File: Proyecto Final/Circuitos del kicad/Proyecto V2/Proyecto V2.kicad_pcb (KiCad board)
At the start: 2 copper layers, 259.8 x 173.7 mm, 43 parts, among them J1 12v, Q1 PN2222A, Q2 PN2222A, Q3 PN2222A, SW1 SW_Push, SW2 SW_Push, SW3 SW_Push, SW4 SW_Push, U1 LM7805, U3 ATmega328P-P, Y1 16MHz

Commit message: Cambios plaqueta
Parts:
- R2, R3, R4: value 1k -> 4k7
- moved D2 10.2 mm to (61.7, 136.7), turned to 180 degrees
- moved D3 10.2 mm to (61.7, 130.0), turned to 180 degrees
- moved D1 10.1 mm to (61.8, 143.5), turned to 180 degrees
- moved Encoder/puls-arduino1 8.63 mm to (17.2, 47.6)
- moved ESP2866-2 7.67 mm to (127.8, 78.9), turned to 90 degrees
- moved Y1 7.17 mm to (31.3, 53.9)
- moved C2 7.08 mm to (27.7, 64.2)
- moved C1 7.08 mm to (27.7, 48.4)
- moved ESP2866-arduino1 6.15 mm to (43.3, 27.9), turned to 90 degrees
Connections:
- D1 pad 1: Net-(D1-Pad1) -> +12V
- D1 pad 2: +12V -> Net-(Q3-Pad3)
- D2 pad 1: Net-(D2-Pad1) -> +12V
- D2 pad 2: +12V -> Net-(Q2-Pad3)
- D3 pad 1: Net-(D3-Pad1) -> +12V
- D3 pad 2: +12V -> Net-(Relay-3-PadA2)
- ESP2866-2 pad 3: Net-(ESP2866-2-Pad3) -> Net-(ESP8266-Pad18)
- ESP8266 pad 18: Net-(ESP2866-2-Pad2) -> Net-(ESP8266-Pad18)
- ESP8266 pad 19: Net-(ESP2866-2-Pad3) -> Net-(ESP2866-2-Pad2)
- Encoder/puls-arduino1 pad 3: Net-(Encoder/puls-arduino1-Pad3) -> Net-(U3-Pad5)
- Encoder/puls-arduino1 pad 5: Net-(Encoder/puls-arduino1-Pad5) -> Net-(U3-Pad4)
- Q1 pad 3: Net-(D3-Pad1) -> Net-(Relay-3-PadA2)
- Q2 pad 3: Net-(D2-Pad1) -> Net-(Q2-Pad3)
- Q3 pad 3: Net-(D1-Pad1) -> Net-(Q3-Pad3)
- Relay-1 pad A1: Net-(D1-Pad1) -> +12V
- Relay-1 pad A2: GND -> Net-(Q3-Pad3)
- Relay-2 pad A1: Net-(D2-Pad1) -> +12V
- Relay-2 pad A2: GND -> Net-(Q2-Pad3)
- Relay-3 pad A1: Net-(D3-Pad1) -> +12V
- Relay-3 pad A2: GND -> Net-(Relay-3-PadA2)
- U3 pad 4: Net-(Encoder/puls-arduino1-Pad3) -> Net-(U3-Pad4)
- U3 pad 5: Net-(Encoder/puls-arduino1-Pad5) -> Net-(U3-Pad5)
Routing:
- net +12V: track 97.9 -> 210.9 mm
- net Net-(D3-Pad1): track 66.6 -> 0.00 mm
- net Net-(Encoder/puls-arduino1-Pad5): track 60.7 -> 0.00 mm
- net Net-(Q3-Pad3): track 0.00 -> 53.4 mm
- net Net-(Encoder/puls-arduino1-Pad3): track 48.3 -> 0.00 mm
- net Net-(U3-Pad4): track 0.00 -> 43.7 mm
- net Net-(D1-Pad1): track 41.8 -> 0.00 mm
- net Net-(U3-Pad5): track 0.00 -> 36.5 mm
- net Net-(Q2-Pad3): track 0.00 -> 35.2 mm
- net Net-(D2-Pad1): track 35.1 -> 0.00 mm
- net Net-(ESP2866-2-Pad3): track 33.3 -> 0.00 mm
- net Net-(Relay-3-PadA2): track 0.00 -> 29.7 mm
- net Net-(ESP8266-Pad18): track 0.00 -> 29.4 mm
- net Net-(Encoder/puls-arduino1-Pad4): track 19.1 -> 27.8 mm
- net Net-(Encoder/puls-arduino1-Pad7): track 142.1 -> 150.7 mm
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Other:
- board size 259.8 x 173.7 mm -> 279.3 x 173.7 mm
- board text added: "+"

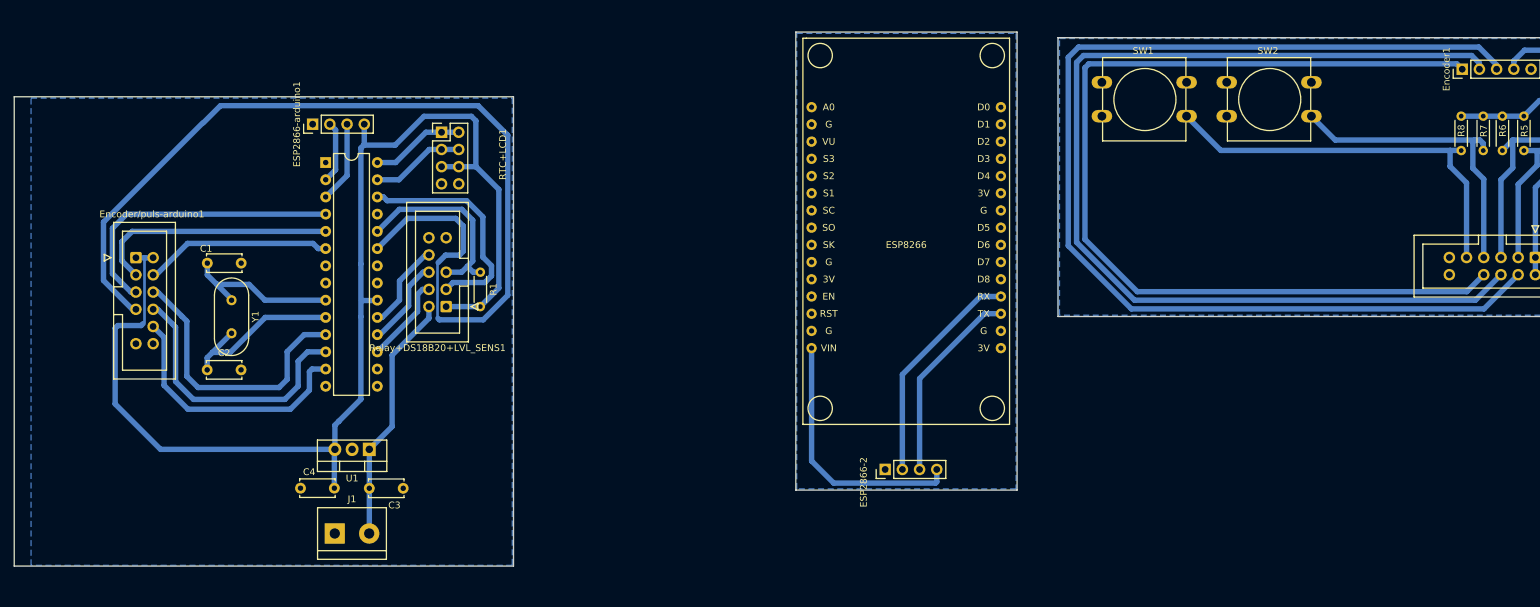
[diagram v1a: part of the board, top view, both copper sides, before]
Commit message: IDC ESP + reset
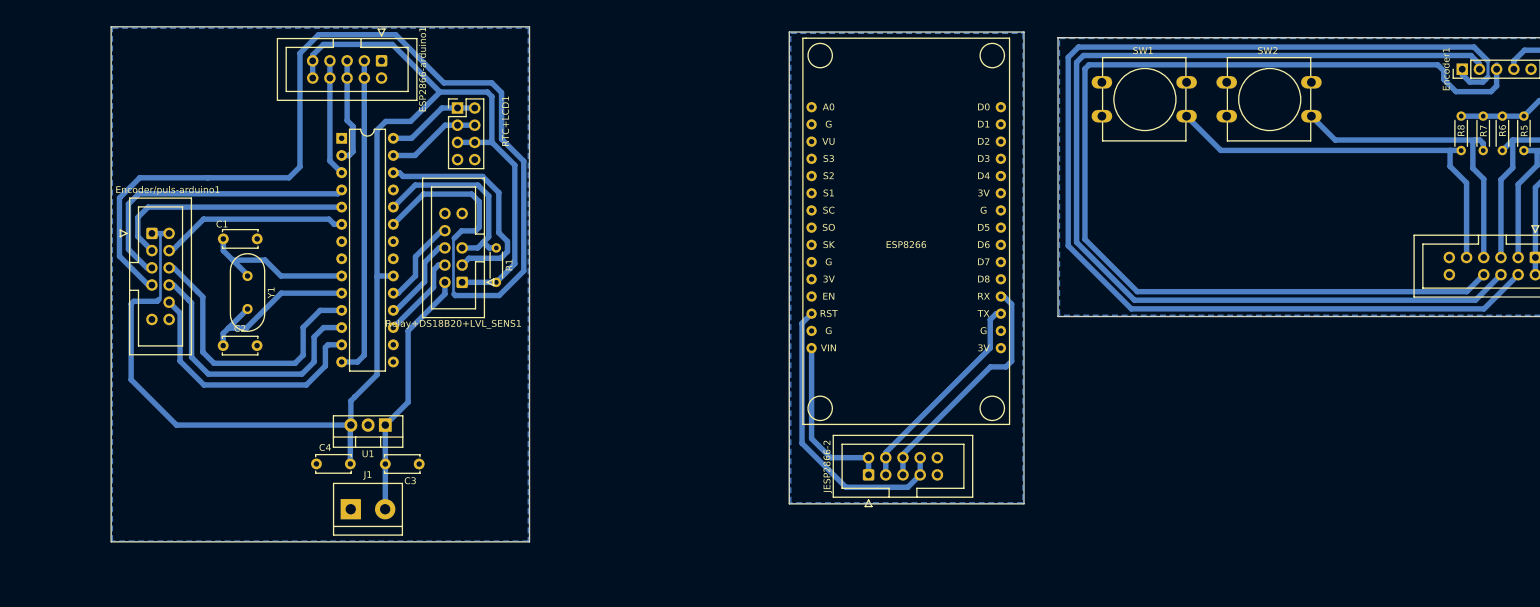
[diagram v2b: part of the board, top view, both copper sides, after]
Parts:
- removed ESP2866-2: Conn_01x04, Connector_PinHeader_2.54mm:PinHeader_1x04_P2.54mm_Vertical
- added JESP2866-2: Conn_02x05_Odd_Even, Connector_IDC:IDC-Header_2x05_P2.54mm_Vertical, F.Cu at (125.3, 79.7)
- ESP2866-arduino1: value Conn_01x04 -> Conn_02x05_Odd_Even; footprint Connector_PinHeader_2.54mm:PinHeader_1x04_P2.54mm_Vertical -> Connector_IDC:IDC-Header_2x05_P2.54mm_Vertical
- moved ESP2866-arduino1 13.8 mm to (53.4, 18.6), turned to -90 degrees
- moved C2 4.29 mm to (30.1, 60.6)
- moved Relay+DS18B20+LVL_SENS1 4.29 mm to (65.3, 51.3)
- moved J1 4.29 mm to (48.9, 84.8)
- moved C1 4.29 mm to (30.1, 44.9)
- moved C3 4.29 mm to (59.0, 78.1)
- moved C4 4.29 mm to (43.8, 78.1)
- moved Encoder/puls-arduino1 4.29 mm to (19.5, 44.0)
- moved R1 4.29 mm to (70.4, 46.2)
- moved RTC+LCD1 4.29 mm to (64.7, 25.5)
- moved U1 4.29 mm to (54.0, 72.3)
- moved U3 4.29 mm to (47.6, 30.0)
- moved Y1 4.29 mm to (33.7, 50.3)
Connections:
- ESP2866-arduino1 pad 2: Net-(ESP2866-arduino1-Pad2) -> GND
- ESP2866-arduino1 pad 3: Net-(ESP2866-arduino1-Pad3) -> Net-(U3-Pad14)
- ESP2866-arduino1 pad 4: +5V -> Net-(U3-Pad14)
- ESP8266 pad 13: unconnected-(ESP8266-Pad13) -> Net-(ESP8266-Pad13)
- Encoder/puls2 pad 4: Net-(Encoder/puls2-Pad4) -> Net-(Encoder1-Pad1)
- Encoder1 pad 1: Net-(Encoder/puls2-Pad8) -> Net-(Encoder1-Pad1)
- Encoder1 pad 3: Net-(Encoder/puls2-Pad4) -> Net-(Encoder/puls2-Pad8)
- U3 pad 14: unconnected-(U3-Pad14) -> Net-(U3-Pad14)
- U3 pad 2: Net-(ESP2866-arduino1-Pad2) -> Net-(U3-Pad2)
- U3 pad 3: Net-(ESP2866-arduino1-Pad3) -> Net-(U3-Pad3)
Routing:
- net Net-(Encoder1-Pad1): track 0.00 -> 171.3 mm
- net Net-(Encoder/puls2-Pad4): track 165.7 -> 0.00 mm
- net Net-(U3-Pad14): track 0.00 -> 47.2 mm
- net Net-(ESP8266-Pad13): track 0.00 -> 43.1 mm
- net Net-(U3-Pad3): track 0.00 -> 17.7 mm
- net Net-(U3-Pad2): track 0.00 -> 15.7 mm
- net Net-(Encoder/puls-arduino1-Pad7): track 150.7 -> 166.1 mm
- net Net-(ESP2866-arduino1-Pad3): track 12.0 -> 0.00 mm
- net Net-(Encoder/puls2-Pad8): track 144.7 -> 155.1 mm
- net +5V: track 570.7 -> 580.0 mm
- net Net-(ESP2866-arduino1-Pad2): track 9.16 -> 0.00 mm
- net Net-(ESP8266-Pad19): track 33.4 -> 35.2 mm
- net Net-(ESP8266-Pad18): track 29.4 -> 31.2 mm
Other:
- board size 279.3 x 173.7 mm -> 265 x 174.5 mm

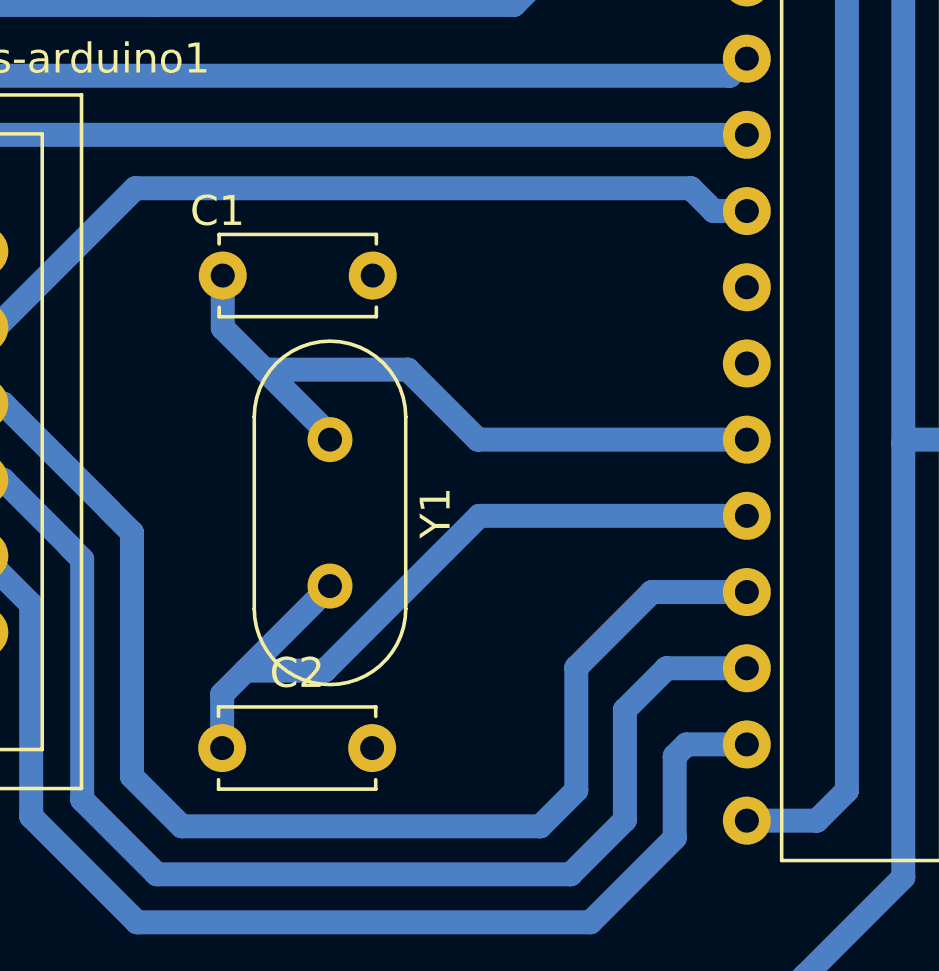
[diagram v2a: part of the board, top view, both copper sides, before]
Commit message: cambio cristal
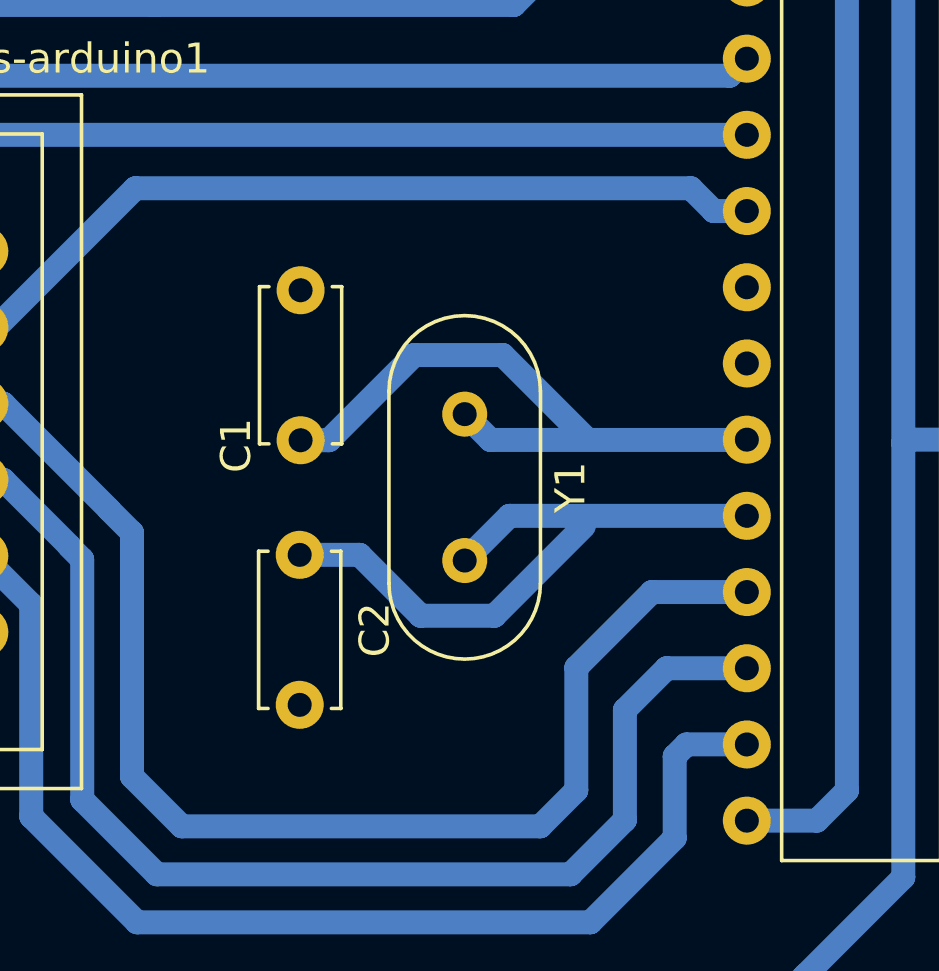
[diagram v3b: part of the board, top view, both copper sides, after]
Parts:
- moved C2 6.94 mm to (32.6, 54.2), turned to -90 degrees
- moved C1 6.07 mm to (32.7, 50.3), turned to 90 degrees
- moved Y1 4.57 mm to (38.1, 49.5)
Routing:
- net Net-(C2-Pad1): track 25.9 -> 21.6 mm
- net Net-(C1-Pad1): track 24.0 -> 21.6 mm
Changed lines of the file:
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@@
   )
   (footprint "Capacitor_THT:C_Disc_D5.0mm_W2.5mm_P5.00mm" (layer "F.Cu")
-    (at 30.065 60.6)
+    (at 32.65 54.16 -90)
     (descr "C, Disc series, Radial, pin pitch=5.00mm, , diameter*width=5*2.5mm^2, Capacitor, http://cdn-reichelt.de/documents/datenblatt/B300/DS_KERKO_TC.pdf")
     (tags "C Disc series Radial pin pitch 5.00mm  diameter 5mm width 2.5mm Capacitor")
@@
     (property "Sheetname" "")
     (attr through_hole)
-    (fp_text reference "C2" (at 2.5 -2.5) (layer "F.SilkS")
-      (effects (font (size 1 1) (thickness 0.15)))
-    )
-    (fp_text value "20pF" (at 2.5 2.5) (layer "F.Fab")
-      (effects (font (size 1 1) (thickness 0.15)))
-    )
-    (fp_text user "${REFERENCE}" (at 2.5 0) (layer "F.Fab")
+    (fp_text reference "C2" (at 2.5 -2.5 90) (layer "F.SilkS")
+      (effects (font (size 1 1) (thickness 0.15)))
+    )
+    (fp_text value "20pF" (at 2.5 2.5 90) (layer "F.Fab")
+      (effects (font (size 1 1) (thickness 0.15)))
+    )
+    (fp_text user "${REFERENCE}" (at 2.5 0 90) (layer "F.Fab")
       (effects (font (size 1 1) (thickness 0.15)))
     )
@@
     (fp_line (start 0 1.25) (end 5 1.25) (layer "F.Fab") (width 0.1))
     (fp_line (start 5 -1.25) (end 0 -1.25) (layer "F.Fab") (width 0.1))
-    (pad "1" thru_hole circle (at 0 0) (size 1.6 1.6) (drill 0.8) (layers *.Cu *.Mask)
+    (pad "1" thru_hole circle (at 0 0 270) (size 1.6 1.6) (drill 0.8) (layers *.Cu *.Mask)
       (net 8 "Net-(C2-Pad1)") (pintype "passive"))
-    (pad "2" thru_hole circle (at 5 0) (size 1.6 1.6) (drill 0.8) (layers *.Cu *.Mask)
+    (pad "2" thru_hole circle (at 5 0 270) (size 1.6 1.6) (drill 0.8) (layers *.Cu *.Mask)
       (net 1 "GND") (pintype "passive"))
     (model "${KICAD6_3DMODEL_DIR}/Capacitor_THT.3dshapes/C_Disc_D5.0mm_W2.5mm_P5.00mm.wrl"
@@
   )
   (footprint "Capacitor_THT:C_Disc_D5.0mm_W2.5mm_P5.00mm" (layer "F.Cu")
-    (at 30.085 44.85)
+    (at 32.68 50.34 90)
     (descr "C, Disc series, Radial, pin pitch=5.00mm, , diameter*width=5*2.5mm^2, Capacitor, http://cdn-reichelt.de/documents/datenblatt/B300/DS_KERKO_TC.pdf")
     (tags "C Disc series Radial pin pitch 5.00mm  diameter 5mm width 2.5mm Capacitor")
@@
     (property "Sheetname" "")
     (attr through_hole)
-    (fp_text reference "C1" (at -0.175 -2.15) (layer "F.SilkS")
-      (effects (font (size 1 1) (thickness 0.15)))
-    )
-    (fp_text value "20pF" (at 2.5 2.5) (layer "F.Fab")
-      (effects (font (size 1 1) (thickness 0.15)))
-    )
-    (fp_text user "${REFERENCE}" (at 2.5 0) (layer "F.Fab")
+    (fp_text reference "C1" (at -0.175 -2.15 90) (layer "F.SilkS")
+      (effects (font (size 1 1) (thickness 0.15)))
+    )
+    (fp_text value "20pF" (at 2.5 2.5 90) (layer "F.Fab")
+      (effects (font (size 1 1) (thickness 0.15)))
+    )
+    (fp_text user "${REFERENCE}" (at 2.5 0 90) (layer "F.Fab")
       (effects (font (size 1 1) (thickness 0.15)))
     )
@@
     (fp_line (start 5 1.25) (end 5 -1.25) (layer "F.Fab") (width 0.1))
     (fp_line (start 0 -1.25) (end 0 1.25) (layer "F.Fab") (width 0.1))
-    (pad "1" thru_hole circle (at 0 0) (size 1.6 1.6) (drill 0.8) (layers *.Cu *.Mask)
+    (pad "1" thru_hole circle (at 0 0 90) (size 1.6 1.6) (drill 0.8) (layers *.Cu *.Mask)
       (net 7 "Net-(C1-Pad1)") (pintype "passive"))
-    (pad "2" thru_hole circle (at 5 0) (size 1.6 1.6) (drill 0.8) (layers *.Cu *.Mask)
+    (pad "2" thru_hole circle (at 5 0 90) (size 1.6 1.6) (drill 0.8) (layers *.Cu *.Mask)
       (net 1 "GND") (pintype "passive"))
     (model "${KICAD6_3DMODEL_DIR}/Capacitor_THT.3dshapes/C_Disc_D5.0mm_W2.5mm_P5.00mm.wrl"
@@
   )
   (footprint "Crystal:Crystal_HC49-4H_Vertical" (layer "F.Cu")
-    (at 33.66 50.32 -90)
+    (at 38.15 49.47 -90)
     (descr "Crystal THT HC-49-4H http://5hertz.com/pdfs/04404_D.pdf")
     (tags "THT crystalHC-49-4H")
@@
   (segment (start 27.5 141.92) (end 39.89 141.92) (width 0.8) (layer "B.Cu") (net 5))
   (segment (start 61.75 143.53) (end 61.75 130.01) (width 0.8) (layer "B.Cu") (net 5))
-  (segment (start 36.255 47.985) (end 38.59 50.32) (width 0.8) (layer "B.Cu") (net 7))
-  (segment (start 38.59 50.32) (end 47.555 50.32) (width 0.8) (layer "B.Cu") (net 7))
+  (segment (start 38.15 49.47) (end 39.01 50.33) (width 0.8) (layer "B.Cu") (net 7))
   (segment (start 47.545 50.33) (end 47.555 50.32) (width 0.8) (layer "B.Cu") (net 7))
-  (segment (start 30.085 46.595) (end 31.475 47.985) (width 0.8) (layer "B.Cu") (net 7))
-  (segment (start 30.085 44.85) (end 30.085 46.595) (width 0.8) (layer "B.Cu") (net 7))
-  (segment (start 31.475 47.985) (end 36.255 47.985) (width 0.8) (layer "B.Cu") (net 7))
-  (segment (start 33.66 50.17) (end 33.66 50.32) (width 0.8) (layer "B.Cu") (net 7))
-  (segment (start 31.475 47.985) (end 33.66 50.17) (width 0.8) (layer "B.Cu") (net 7))
-  (segment (start 33.66 55.21) (end 33.66 55.2) (width 0.8) (layer "B.Cu") (net 8))
-  (segment (start 30.85 58.02) (end 33.66 55.21) (width 0.8) (layer "B.Cu") (net 8))
-  (segment (start 30.065 60.6) (end 30.065 58.805) (width 0.8) (layer "B.Cu") (net 8))
-  (segment (start 30.175 60.71) (end 30.065 60.6) (width 0.8) (layer "B.Cu") (net 8))
-  (segment (start 33.48 58.02) (end 38.64 52.86) (width 0.8) (layer "B.Cu") (net 8))
-  (segment (start 38.64 52.86) (end 47.555 52.86) (width 0.8) (layer "B.Cu") (net 8))
-  (segment (start 30.85 58.02) (end 33.48 58.02) (width 0.8) (layer "B.Cu") (net 8))
-  (segment (start 30.065 58.805) (end 30.85 58.02) (width 0.8) (layer "B.Cu") (net 8))
+  (segment (start 36.465 47.5) (end 39.42 47.5) (width 0.8) (layer "B.Cu") (net 7))
+  (segment (start 39.01 50.33) (end 47.545 50.33) (width 0.8) (layer "B.Cu") (net 7))
+  (segment (start 39.42 47.5) (end 42.2 50.28) (width 0.8) (layer "B.Cu") (net 7))
+  (segment (start 32.68 50.34) (end 33.625 50.34) (width 0.8) (layer "B.Cu") (net 7))
+  (segment (start 33.625 50.34) (end 36.465 47.5) (width 0.8) (layer "B.Cu") (net 7))
+  (segment (start 38.15 54.35) (end 39.64 52.86) (width 0.8) (layer "B.Cu") (net 8))
+  (segment (start 34.65 54.16) (end 36.68 56.19) (width 0.8) (layer "B.Cu") (net 8))
+  (segment (start 39.64 52.86) (end 47.555 52.86) (width 0.8) (layer "B.Cu") (net 8))
+  (segment (start 36.68 56.19) (end 39.14 56.19) (width 0.8) (layer "B.Cu") (net 8))
+  (segment (start 32.65 54.16) (end 34.65 54.16) (width 0.8) (layer "B.Cu") (net 8))
+  (segment (start 39.14 56.19) (end 42.12 53.21) (width 0.8) (layer "B.Cu") (net 8))
+  (segment (start 38.15 54.36) (end 38.15 54.35) (width 0.8) (layer "B.Cu") (net 8))
   (segment (start 41.05 130.61) (end 41.06 130.6) (width 0.8) (layer "B.Cu") (net 9))
   (segment (start 41.06 130.6) (end 45.97 130.6) (width 0.8) (layer "B.Cu") (net 9))
